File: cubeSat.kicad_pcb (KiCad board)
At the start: 2 copper layers, 67 x 68 mm, 0 parts

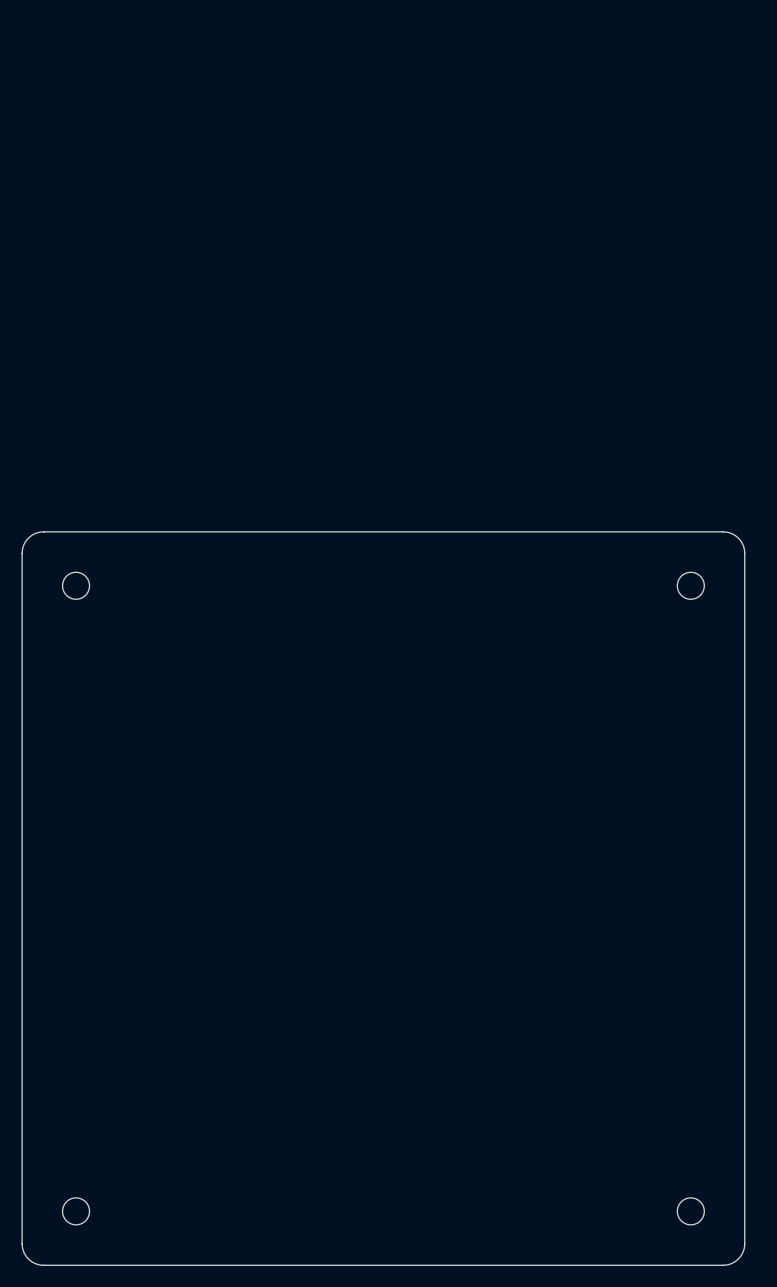
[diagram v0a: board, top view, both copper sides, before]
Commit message: ESP_DHT_added
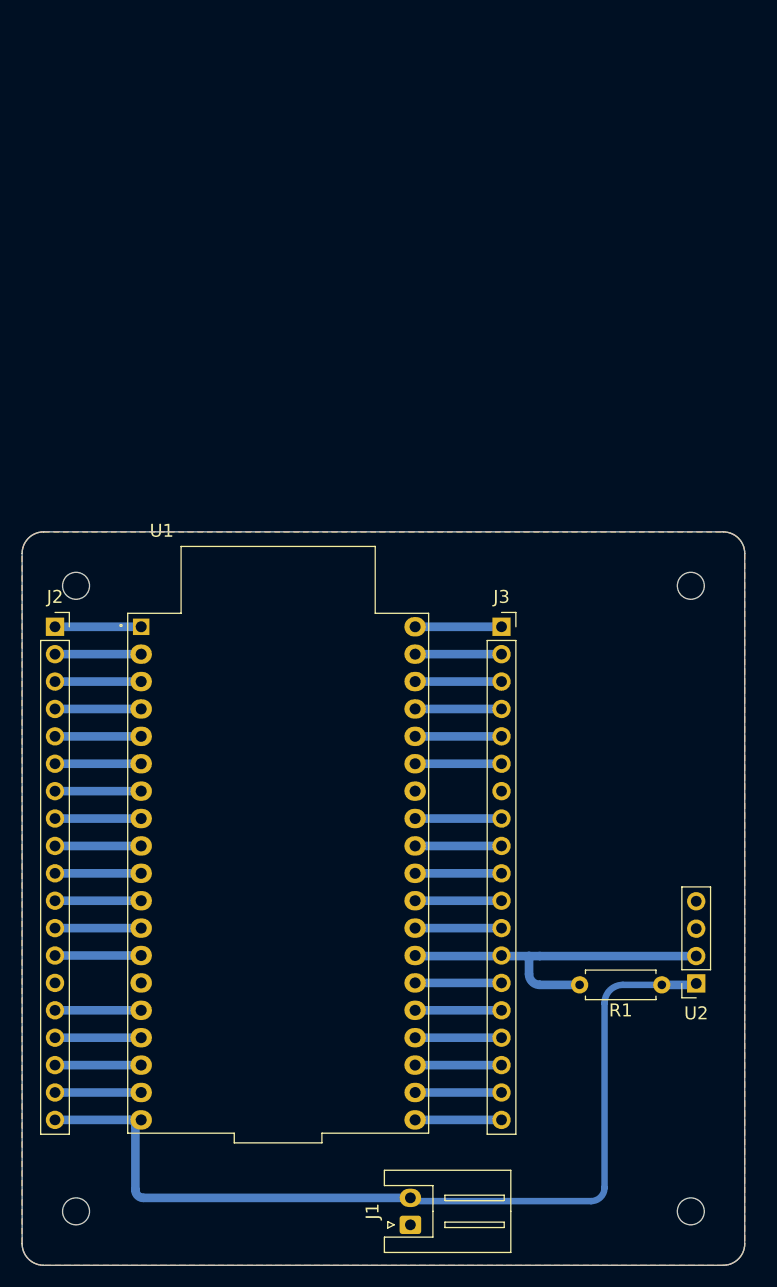
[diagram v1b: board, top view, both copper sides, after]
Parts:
- added J1: VCC_5V_9V_DC, Connector_JST:JST_XH_S2B-XH-A_1x02_P2.50mm_Horizontal, F.Cu at (95.5, 159.2)
- added J2: Conn_01x19, Connector_PinSocket_2.54mm:PinSocket_1x19_P2.54mm_Vertical, F.Cu at (62.5, 103.8)
- added J3: Conn_01x19, Connector_PinSocket_2.54mm:PinSocket_1x19_P2.54mm_Vertical, F.Cu at (104.0, 103.8)
- added R1: 5K_1/4W_THT, Resistor_THT:R_Axial_DIN0207_L6.3mm_D2.5mm_P7.62mm_Horizontal, F.Cu at (118.8, 137.0)
- added U1: DEVKIT_V1_ESP32-WROOM-32, fevino:MODULE_DEVKIT_V1_ESP32-WROOM-32, F.Cu at (83.2, 126.7)
- added U2: ~, Connector_PinSocket_2.54mm:PinSocket_1x04_P2.54mm_Vertical, F.Cu at (122.0, 136.9)
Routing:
- net /SRC/VCC_5V: track 0.00 -> 85.8 mm
- net /SRC/DHT11_1: track 0.00 -> 33.0 mm
- net Net-(J3-Pin_9): track 0.00 -> 8.01 mm
- net Net-(J3-Pin_8): track 0.00 -> 8.01 mm
- net Net-(J3-Pin_6): track 0.00 -> 8.01 mm
- net Net-(J3-Pin_5): track 0.00 -> 8.01 mm
- net Net-(J3-Pin_4): track 0.00 -> 8.01 mm
- net Net-(J3-Pin_3): track 0.00 -> 8.01 mm
- net Net-(J3-Pin_2): track 0.00 -> 8.01 mm
- net Net-(J3-Pin_19): track 0.00 -> 8.01 mm
- net Net-(J3-Pin_18): track 0.00 -> 8.01 mm
- net Net-(J3-Pin_17): track 0.00 -> 8.01 mm
- net Net-(J3-Pin_16): track 0.00 -> 8.01 mm
- net Net-(J3-Pin_15): track 0.00 -> 8.01 mm
- net Net-(J3-Pin_12): track 0.00 -> 8.01 mm
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- added copper zone on B.Cu, net /SRC/GND
- added copper zone on F.Cu, net /SRC/GND

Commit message: added dimensions
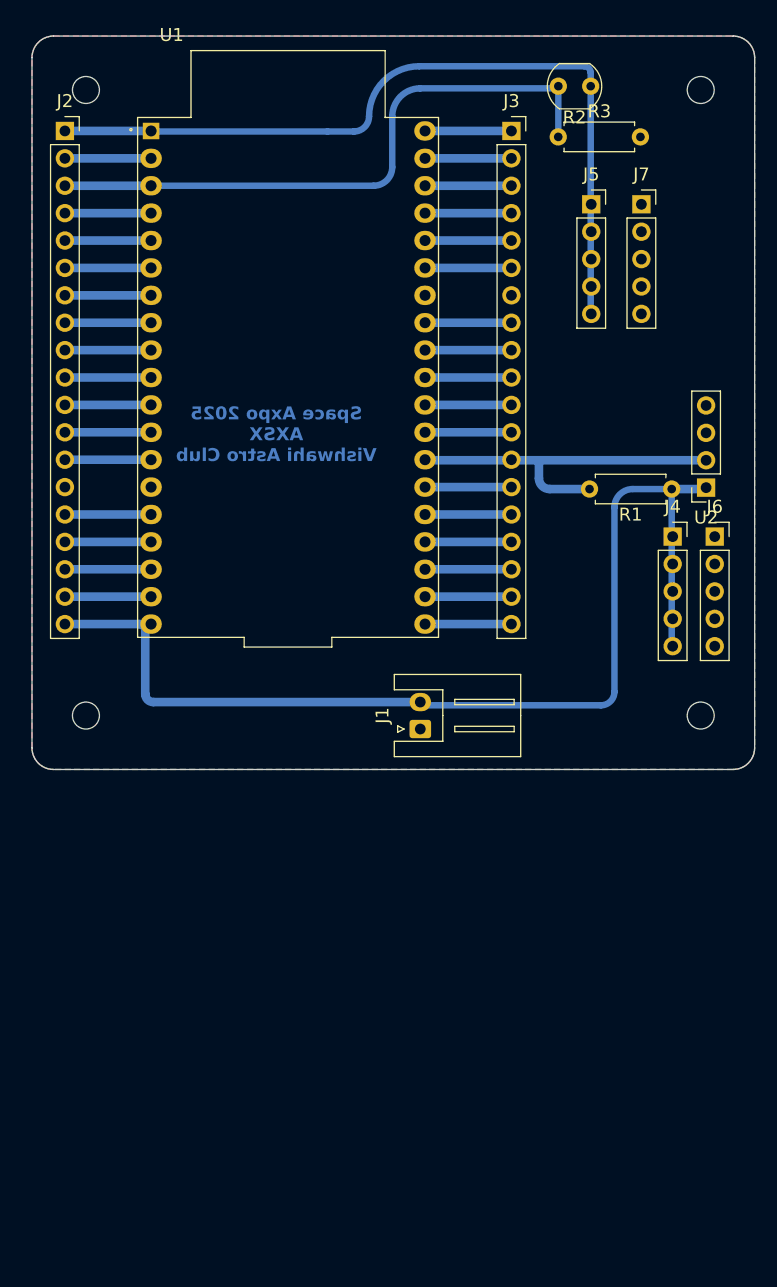
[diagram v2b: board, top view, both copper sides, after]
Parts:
- added J4: Conn_01x05, Connector_PinSocket_2.54mm:PinSocket_1x05_P2.54mm_Vertical, F.Cu at (119.8, 95.4)
- added J5: Conn_01x05, Connector_PinSocket_2.54mm:PinSocket_1x05_P2.54mm_Vertical, F.Cu at (112.3, 64.6)
- added J6: Conn_01x05, Connector_PinSocket_2.54mm:PinSocket_1x05_P2.54mm_Vertical, F.Cu at (123.7, 95.4)
- added J7: Conn_01x05, Connector_PinSocket_2.54mm:PinSocket_1x05_P2.54mm_Vertical, F.Cu at (116.9, 64.6)
- added R2: LDR, OptoDevice:R_LDR_5.0x4.1mm_P3mm_Vertical, F.Cu at (112.2, 53.7)
- added R3: 5K_1/4W_THT, Resistor_THT:R_Axial_DIN0207_L6.3mm_D2.5mm_P7.62mm_Horizontal, F.Cu at (109.2, 58.4)
- moved J1 46.0 mm to (96.4, 113.3)
- moved J2 46.0 mm to (63.5, 57.8)
- moved J3 46.0 mm to (104.9, 57.8)
- moved R1 46.0 mm to (119.7, 91.0)
- moved U1 46.0 mm to (84.2, 80.7)
- moved U2 46.0 mm to (122.9, 90.9)
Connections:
- net Net-(J2-Pin_1) renamed /SRC/VCC_3V3
- net Net-(J2-Pin_3) renamed /SRC/LDR_in
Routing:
- net /SRC/VCC_3V3: track 7.99 -> 74.7 mm
- net /SRC/LDR_in: track 7.99 -> 57.6 mm
- net /SRC/VCC_5V: track 85.8 -> 100.4 mm
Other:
- board text added: "0"
- board text added: "0 mm"
- board text added: "0.01 mm"
- board text added: "0.02"
- board text added: "0.035 mm"
- board text added: "0.1800 mm / 0.1800 mm"
- board text added: "0.2000 mm"
- board text added: "1"
- board text added: "1.5 mm"
- board text added: "1.5900 mm"
- board text added: "2"
- board text added: "3.8"
- board text added: "4.5"
- board text added: "67.0000 mm x 68.0000 mm"
- board text added: "B.Cu"
- board text added: "B.Mask"
- board text added: "B.Paste"
- board text added: "B.Silkscreen"
- board text added: "BOARD CHARACTERISTICS"
- board text added: "Blue"
- board text added: "Board Thickness:"
- board text added: "Board overall dimensions:"
- board text added: "Bottom Silk Screen"
- board text added: "Bottom Solder Mask"
- board text added: "Bottom Solder Paste"
- board text added: "Castellated pads:"
- board text added: "Color"
- board text added: "Copper Finish:"
- board text added: "Copper Layer Count:"
- board text added: "Dielectric"
- board text added: "Edge card connectors:"
- board text added: "Epsilon R"
- board text added: "F.Cu"
- board text added: "F.Mask"
- board text added: "F.Paste"
- board text added: "F.Silkscreen"
- board text added: "FR4"
- board text added: "FR4 natural"
- board text added: "General"
- board text added: "HAL lead-free"
- board text added: "Impedance Control:"
- board text added: "Layer Name"
- board text added: "Loss Tangent"
- board text added: "Material"
- board text added: "Min hole diameter:"
- board text added: "Min track/spacing:"
- board text added: "No"
- board text added: "Plated Board Edge:"
- board text added: "Space Axpo 2025 AXSX Vishwahi Astro Club"
- board text added: "Thickness (mm)"
- board text added: "Top Silk Screen"
- board text added: "Top Solder Mask"
- board text added: "Top Solder Paste"
- board text added: "Type"
- board text added: "White"
- board text added: "copper"
- board text added: "core"

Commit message: copy_first
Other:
- board text added: "3V3"
- board text added: "5V"
- board text added: "GND"
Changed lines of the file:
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@@
 		(at 84.157547 80.68)
 		(property "Reference" "U1"
-			(at -10.795 -31.75 0)
+			(at -0.24 26.2126 0)
 			(layer "F.SilkS")
 			(effects
@@
 		(tags "Resistor Axial_DIN0207 series Axial Horizontal pin pitch 7.62mm 0.25W = 1/4W length 6.3mm diameter 2.5mm")
 		(property "Reference" "R1"
-			(at 3.81 -2.37 0)
+			(at 3.81 2.4626 0)
 			(layer "F.SilkS")
 			(effects
@@
 		(tags "Resistor LDR5x4.1mm")
 		(property "Reference" "R2"
-			(at 1.5 -2.9 0)
+			(at 1.5 3.2626 0)
 			(layer "F.SilkS")
 			(effects
@@
 		(tags "Through hole socket strip THT 1x04 2.54mm single row")
 		(property "Reference" "U2"
-			(at 0 -2.77 0)
+			(at -0.025 10.3626 0)
 			(layer "F.SilkS")
 			(effects
@@
 		(tags "Resistor Axial_DIN0207 series Axial Horizontal pin pitch 7.62mm 0.25W = 1/4W length 6.3mm diameter 2.5mm")
 		(property "Reference" "R3"
-			(at 3.81 -2.37 0)
+			(at 5.31 -2.4626 0)
 			(layer "F.SilkS")
 			(effects
@@
 		(tags "connector JST XH horizontal")
 		(property "Reference" "J1"
-			(at 1.25 -3.51 90)
+			(at 6.588572 3.445 90)
 			(layer "F.SilkS")
 			(effects
@@
 		(tags "Through hole socket strip THT 1x05 2.54mm single row")
 		(property "Reference" "J4"
-			(at 0 -2.77 0)
+			(at -0.025 12.8626 0)
 			(layer "F.SilkS")
 			(effects
@@
 		(tags "Through hole socket strip THT 1x05 2.54mm single row")
 		(property "Reference" "J6"
-			(at 0 -2.77 0)
+			(at -0.025 12.8626 0)
 			(layer "F.SilkS")
 			(effects
@@
 		(tags "Through hole socket strip THT 1x05 2.54mm single row")
 		(property "Reference" "J5"
-			(at 0 -2.77 0)
+			(at -0.025 -2.7626 0)
 			(layer "F.SilkS")
 			(effects
@@
 		(tags "Through hole socket strip THT 1x19 2.54mm single row")
 		(property "Reference" "J2"
-			(at 0 -2.77 0)
+			(at -0.025 48.4626 0)
 			(layer "F.SilkS")
 			(effects
@@
 		(tags "Through hole socket strip THT 1x19 2.54mm single row")
 		(property "Reference" "J3"
-			(at 0 -2.77 0)
+			(at -0.025 -2.7626 0)
 			(layer "F.SilkS")
 			(effects
@@
 		(tags "Through hole socket strip THT 1x05 2.54mm single row")
 		(property "Reference" "J7"
-			(at 0 -2.77 0)
+			(at -0.025 -2.7626 0)
 			(layer "F.SilkS")
 			(effects
@@
 		)
 	)
+	(gr_text "GND\n"
+		(at 117.5 80.5 90)
+		(layer "F.SilkS")
+		(effects
+			(font
+				(size 1.2 1.2)
+				(thickness 0.12)
+			)
+			(justify left bottom)
+		)
+	)
+	(gr_text "3V3\n"
+		(at 113 80 90)
+		(layer "F.SilkS")
+		(effects
+			(font
+				(size 1.2 1.2)
+				(thickness 0.12)
+			)
+			(justify left bottom)
+		)
+	)
+	(gr_text "GND\n"
+		(at 119 113 90)
+		(layer "F.SilkS")
+		(effects
+			(font
+				(size 1.2 1.2)
+				(thickness 0.12)
+			)
+			(justify left bottom)
+		)
+	)
+	(gr_text "5V\n"
+		(at 117 111.5 90)
+		(layer "F.SilkS")
+		(effects
+			(font
+				(size 1.2 1.2)
+				(thickness 0.12)
+			)
+			(justify left bottom)
+		)
+	)

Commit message: increased clearance for pcb manufacturing
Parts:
- U2: value ~ -> DHT11 module 4 pin
- moved J5 9.23 mm to (121.5, 64.6)
- moved R3 3.29 mm to (112.5, 58.4), turned to -90 degrees
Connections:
- J1 pad 1: /SRC/GND -> /SRC/VCC_5V
- J1 pad 2: /SRC/VCC_5V -> /SRC/GND
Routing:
- net /SRC/GND: track 8.01 -> 110.0 mm
- net /SRC/VCC_3V3: track 74.7 -> 85.5 mm
- net /SRC/LDR_in: track 57.6 -> 61.8 mm
- net /SRC/VCC_5V: track 100.4 -> 103.3 mm
